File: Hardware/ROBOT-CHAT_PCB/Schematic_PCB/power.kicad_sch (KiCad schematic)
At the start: 15 parts, among them J5 Conn_01x02

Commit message: Merge PCB v3
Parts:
- added C301: 22u, Capacitor_SMD:C_0805_2012Metric, symbol Device:C_Small
- added J6: Conn_01x02, Connector_JST:JST_PH_B2B-PH-K_1x02_P2.00mm_Vertical, symbol Connector_Generic:Conn_01x02
- added R301: 100k, Resistor_SMD:R_0402_1005Metric, symbol Device:R_Small
- BU33SD5WG-TR1: footprint BU33SD5WG-TR:BU33SD5WG-TR -> Package_TO_SOT_SMD:SOT-23-5
- C1, C2: footprint (none) -> Capacitor_SMD:C_0603_1608Metric
- C19, C20: value 0,1uF -> 100n; footprint (none) -> Capacitor_SMD:C_0402_1005Metric
- C22: footprint (none) -> Capacitor_SMD:C_0805_2012Metric
- C23: value 47uF -> 22u; footprint (none) -> Capacitor_SMD:C_0805_2012Metric
- J5: footprint (none) -> Connector_JST:JST_PH_B2B-PH-K_1x02_P2.00mm_Vertical
- L3: value 4,7uH -> 4.7uH; footprint (none) -> Bobine_74404054068:Bobine_74404054068
- R1, R2, R7, R8: footprint (none) -> Resistor_SMD:R_0402_1005Metric
- R9: value 40,2k -> 40.2k; footprint (none) -> Resistor_SMD:R_0402_1005Metric
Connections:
- net EN3.3 is gone; now on net +5V: BU33SD5WG-TR1.3 (STBY)
- net +5V: now also C301.2
- net GND: now also J5.1 (Pin_1), C301.1; no longer J5.2 (Pin_2)
- net VCC: now reaches C20.1, MP1475DJ-LF-P1.7 (VCC), R7.1
- net PG: now reaches MP1475DJ-LF-P1.1 (PG), R7.2
- net SW: now reaches C19.2, L3.1, MP1475DJ-LF-P1.3 (SW)
- net BST: now reaches MP1475DJ-LF-P1.5 (BST), R8.1
- net FB: now reaches MP1475DJ-LF-P1.8 (FB), R1.1
- net EN5 renamed EN
- net EN: now also R301.2
- net VIN renamed +7.2V
- net +7.2V: now also J6.2 (Pin_2), R301.1
- new net Vbatt+: J5.2 (Pin_2), J6.1 (Pin_1)
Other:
- note added: "Batterie"
- note added: "Interrupteur"
- moved on the sheet: C1, C2

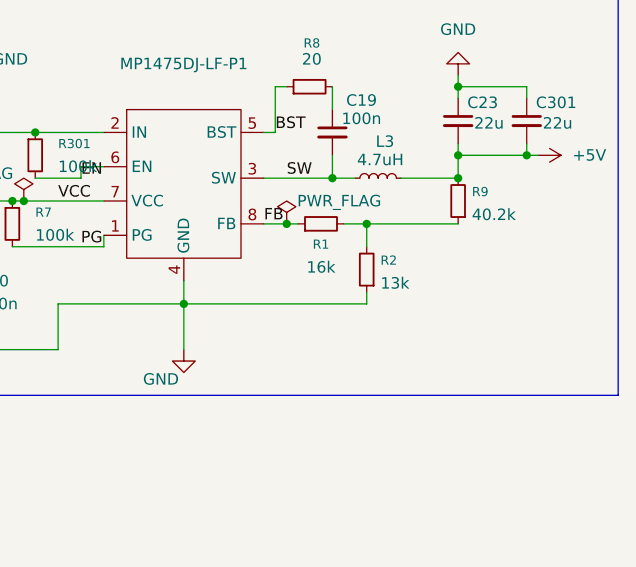
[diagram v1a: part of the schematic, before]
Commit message: Deleted antenna space btw signals and change R2 value
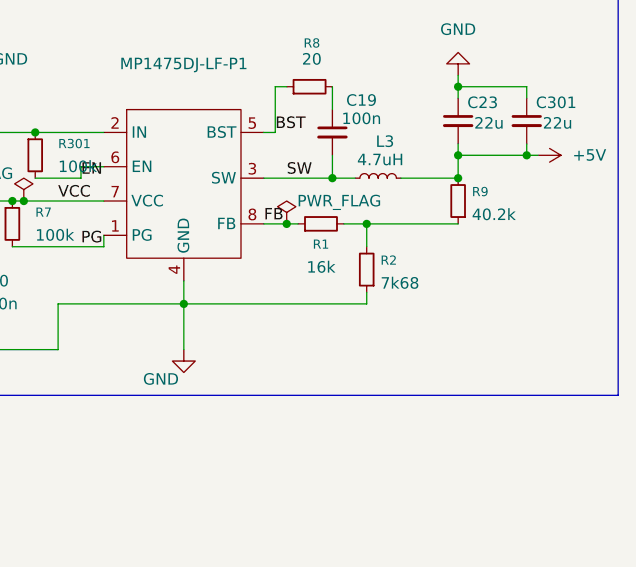
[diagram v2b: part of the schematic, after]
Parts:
- R2: value 13k -> 7k68
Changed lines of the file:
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@@
 			)
 		)
-		(property "Value" "13k"
+		(property "Value" "7k68"
 			(at 249.174 52.324 0)
 			(effects
